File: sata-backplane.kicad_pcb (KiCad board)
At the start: 4 copper layers, 56 x 43 mm, 11 parts, among them J1 SATA_POWER_15, J10 SATA_1, J11 SATA_COMBINED_1, J20 SATA_2, J21 SATA_COMBINED_2

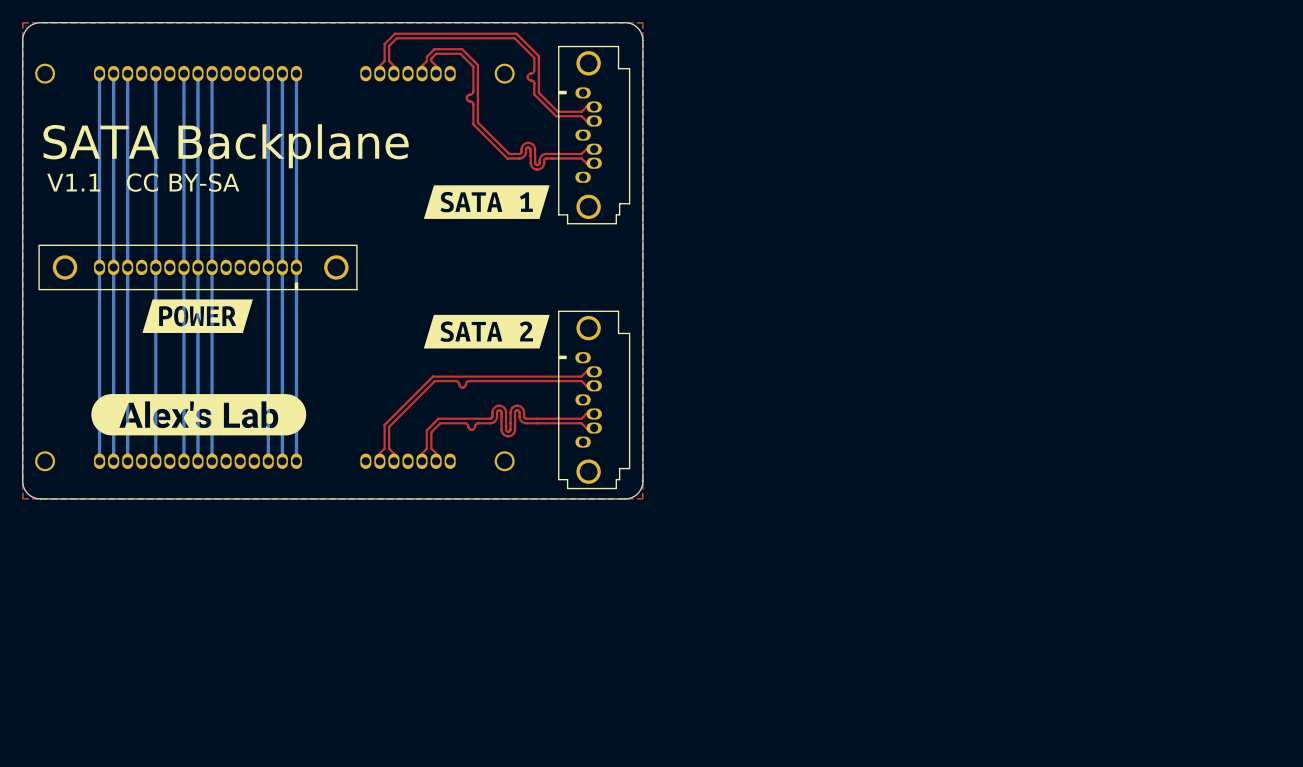
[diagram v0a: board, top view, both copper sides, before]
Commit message: Modified PCB to fit the AX700 Drive Cages
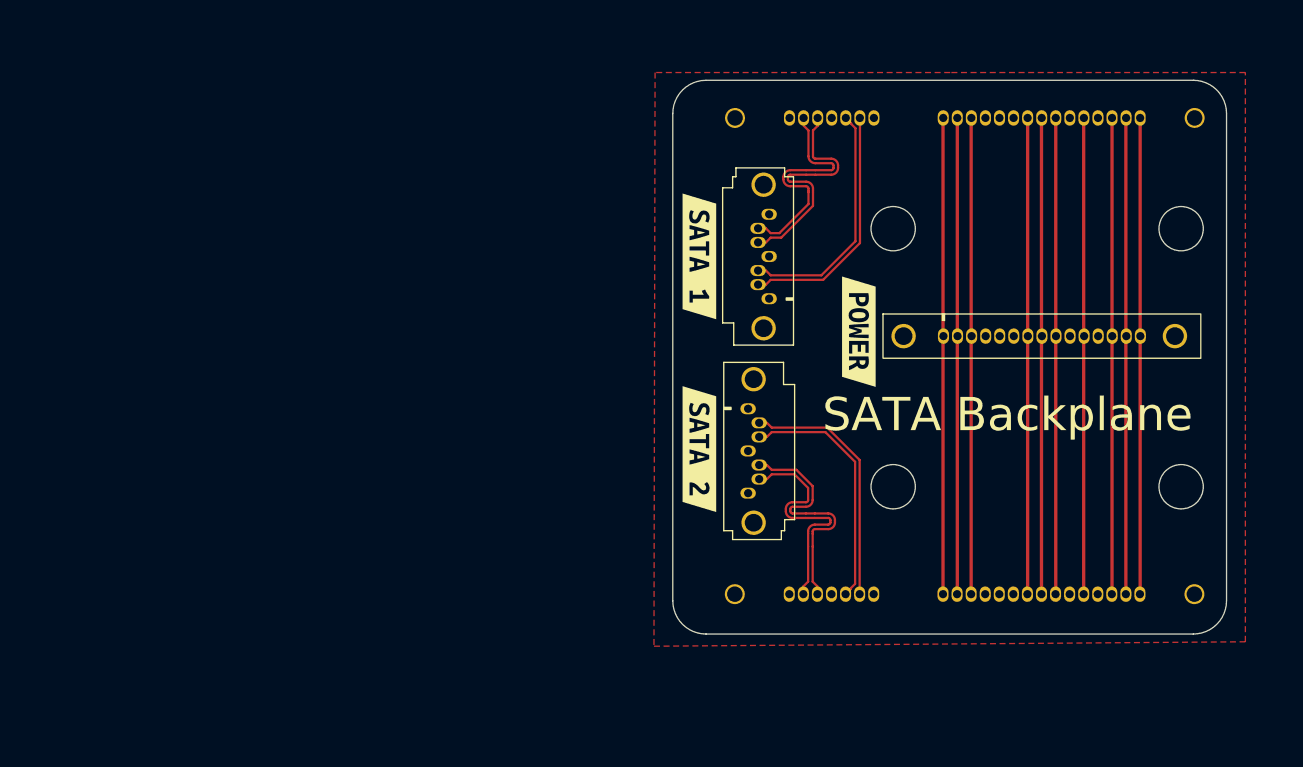
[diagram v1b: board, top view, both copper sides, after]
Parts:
- removed kibuzzard-63B1B127: G***, kibuzzard-63B1B127
- moved kibuzzard-63B1B180 59.7 mm to (96.9, 47.3), turned to -90 degrees
- moved J1 58.7 mm to (104.5, 47.7), turned to 0 degrees
- moved kibuzzard-63B1B17B 50.7 mm to (106.0, 65.3)
- moved kibuzzard-63B1B175 49.8 mm to (106.0, 33.6)
- moved J21 32.9 mm to (90.6, 71.0), turned to 0 degrees
- moved J11 30.9 mm to (90.6, 28.0), turned to 0 degrees
- moved kibuzzard-63B1B17B 21.9 mm to (82.5, 57.9), turned to -90 degrees
- moved kibuzzard-63B1B175 19.8 mm to (82.5, 40.5), turned to -90 degrees
- moved J10 17.1 mm to (88.8, 36.7), turned to 90 degrees
- moved J20 15.6 mm to (86.9, 61.9)
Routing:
- net /5V_3: track 35.0 -> 43.0 mm
- net /3V3_2: track 35.0 -> 43.0 mm
- net /12V_1: track 35.0 -> 43.0 mm
- net /PWDIS: track 35.0 -> 43.0 mm
- net /ACT: track 35.0 -> 43.0 mm
- net /5V_2: track 35.0 -> 43.0 mm
- net /5V_1: track 35.0 -> 43.0 mm
- net /3V3_1: track 35.0 -> 43.0 mm
- net /12V_3: track 35.0 -> 43.0 mm
- net /12V_2: track 35.0 -> 43.0 mm
- net /SATA1_A+: track 27.1 -> 21.6 mm
- net /SATA1_B-: track 27.1 -> 21.7 mm
- net /SATA1_B+: track 27.2 -> 22.0 mm
- net /SATA1_A-: track 27.1 -> 22.3 mm
- net /SATA2_A+: track 24.2 -> 21.8 mm
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- removed copper zone on B.Cu, net GND
- removed copper zone on In1.Cu, net GND
- removed copper zone on In2.Cu, net GND
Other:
- board size 56 x 43 mm -> 50 x 50 mm
- board text removed: "Board infos: 4 Layers / 1.6 mm +- 10% Top/Bottom Layer: 0.035 mm copper Prepreg 7628"
- board text removed: "Controlled impedance: Layer 1 ref layer 2, 100 +- 10% ohm diff: 0.205 mm trace, 0.2032 mm space Layer 4 ref layer 3, 100 +- 10% ohm diff: 0.205 mm trace, 0.2032 mm space"
- board text removed: "JLCJLCJLCJLC"
- board text removed: "S/N:"
- board text removed: "V1.1 CC BY-SA"

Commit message: Done, New parts & spacing
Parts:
- removed J10: SATA_1, sata:SATA_Data
- removed J11: SATA_COMBINED_1, sata:SATA_Combined
- removed J20: SATA_2, sata:SATA_Data
- removed J21: SATA_COMBINED_2, sata:SATA_Combined
- removed kibuzzard-63B1B180: G***, kibuzzard-63B1B180
- added H1: MountingHole_Pad, MountingHole:MountingHole_3.2mm_M3_Pad_TopBottom, F.Cu at (66.8, 45.1)
- added H2: MountingHole_Pad, MountingHole:MountingHole_3.2mm_M3_Pad_TopBottom, F.Cu at (117.1, 50.4)
- added H3: MountingHole_Pad, MountingHole:MountingHole_3.2mm_M3_Pad_TopBottom, F.Cu at (117.1, 68.0)
- added H4: MountingHole_Pad, MountingHole:MountingHole_3.2mm_M3_Pad_TopBottom, F.Cu at (66.8, 73.9)
- added J2: 877791001, CONN_877791001_MOL:CONN_877791001_MOL, B.Cu at (72.3, 81.6)
- added J3: 470804001, CONN_47080-4001_MOL:CONN_47080-4001_MOL, F.Cu at (128.0, 43.1)
- added J4: 877791001, CONN_877791001_MOL:CONN_877791001_MOL, B.Cu at (72.3, 37.6)
- added J5: SATA_POWER_15, sata:SATA_Power, F.Cu at (84.4, 68.1)
- J1: value SATA_POWER_15 -> 470804001; footprint sata:SATA_Power -> CONN_47080-4001_MOL:CONN_47080-4001_MOL
- moved kibuzzard-63B1B17B 51.0 mm to (56.2, 76.5)
- moved kibuzzard-63B1B175 50.5 mm to (56.2, 42.5)
- moved kibuzzard-63B1B175 47.2 mm to (127.6, 54.5), turned to 0 degrees
- moved kibuzzard-63B1B17B 45.3 mm to (127.5, 62.7), turned to 0 degrees
- moved J1 36.3 mm to (128.0, 75.3), turned to 90 degrees
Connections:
- J1 pad 1: /3V3_1 -> GND
- J1 pad 2: /3V3_2 -> /SATA1_A+
- J1 pad 3: /PWDIS -> /SATA1_A-
- J1 pad 5: GND -> /SATA1_B+
- J1 pad 6: GND -> /SATA1_B-
- J1 pad 7: /5V_1 -> GND
- J1 pad 8: /5V_2 -> (no net)
- J1 pad 9: /5V_3 -> (no net)
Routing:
- net /12V_B: track 0.00 -> 87.8 mm, vias 0 -> 1
- net /12V_A: track 0.00 -> 86.6 mm, vias 0 -> 1
- net /12V_PRE: track 0.00 -> 85.3 mm, vias 0 -> 1
- net /SS/ACT: track 0.00 -> 82.8 mm, vias 0 -> 1
- net /5V_B: track 0.00 -> 80.2 mm, vias 0 -> 1
- net /5V_A: track 0.00 -> 78.9 mm, vias 0 -> 1
- net /5V_PRE: track 0.00 -> 77.7 mm, vias 0 -> 1
- net /PW_DIS: track 0.00 -> 72.6 mm, vias 0 -> 1
- net /3V3_B: track 0.00 -> 71.3 mm, vias 0 -> 1
- net /3V3_A: track 0.00 -> 70.1 mm, vias 0 -> 1
- net /SATA1_B-: track 21.7 -> 64.8 mm
- net /5V_3: track 43.0 -> 0.00 mm
- net /3V3_2: track 43.0 -> 0.00 mm
- net /12V_1: track 43.0 -> 0.00 mm
- net /PWDIS: track 43.0 -> 0.00 mm
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- added copper zone on B.Cu, net GND
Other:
- board size 50 x 50 mm -> 100 x 50.8 mm
- board text removed: "SATA Backplane"

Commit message: DRC foxes for PCBway
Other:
- copper layers 4 -> 2
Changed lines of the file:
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@@
 	(layers
 		(0 "F.Cu" signal)
-		(4 "In1.Cu" signal)
-		(6 "In2.Cu" signal)
 		(2 "B.Cu" signal)
 		(9 "F.Adhes" user "F.Adhesive")
@@
 			)
 			(layer "dielectric 1"
-				(type "prepreg")
-				(thickness 0.2104)
-				(material "FR4")
-				(epsilon_r 4.6)
-				(loss_tangent 0.02)
-			)
-			(layer "In1.Cu"
-				(type "copper")
-				(thickness 0.0152)
-			)
-			(layer "dielectric 2"
 				(type "core")
-				(thickness 1.065)
-				(material "FR4")
-				(epsilon_r 4.5)
-				(loss_tangent 0.02)
-			)
-			(layer "In2.Cu"
-				(type "copper")
-				(thickness 0.0152)
-			)
-			(layer "dielectric 3"
-				(type "prepreg")
-				(thickness 0.2104)
+				(thickness 1.5162)
 				(material "FR4")
 				(epsilon_r 4.6)
@@
 		(single_sided no)
 		(target_length 65)
-		(target_length_max 65.1)
+		(target_length_max 65.099999)
 		(target_length_min 64.9)
 		(target_skew 0)
@@
 		(single_sided no)
 		(target_length 65)
-		(target_length_max 65.1)
+		(target_length_max 65.099999)
 		(target_length_min 64.9)
 		(target_skew 0)
@@
 		(single_sided no)
 		(target_length 65)
-		(target_length_max 65.1)
+		(target_length_max 65.099999)
 		(target_length_min 64.9)
 		(target_skew 0)
@@
 		(single_sided no)
 		(target_length 65)
-		(target_length_max 65.1)
+		(target_length_max 65.099999)
 		(target_length_min 64.9)
 		(target_skew 0)
